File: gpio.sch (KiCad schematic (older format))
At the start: 1 part, among them U1 LFE5U-85F-6BG381C

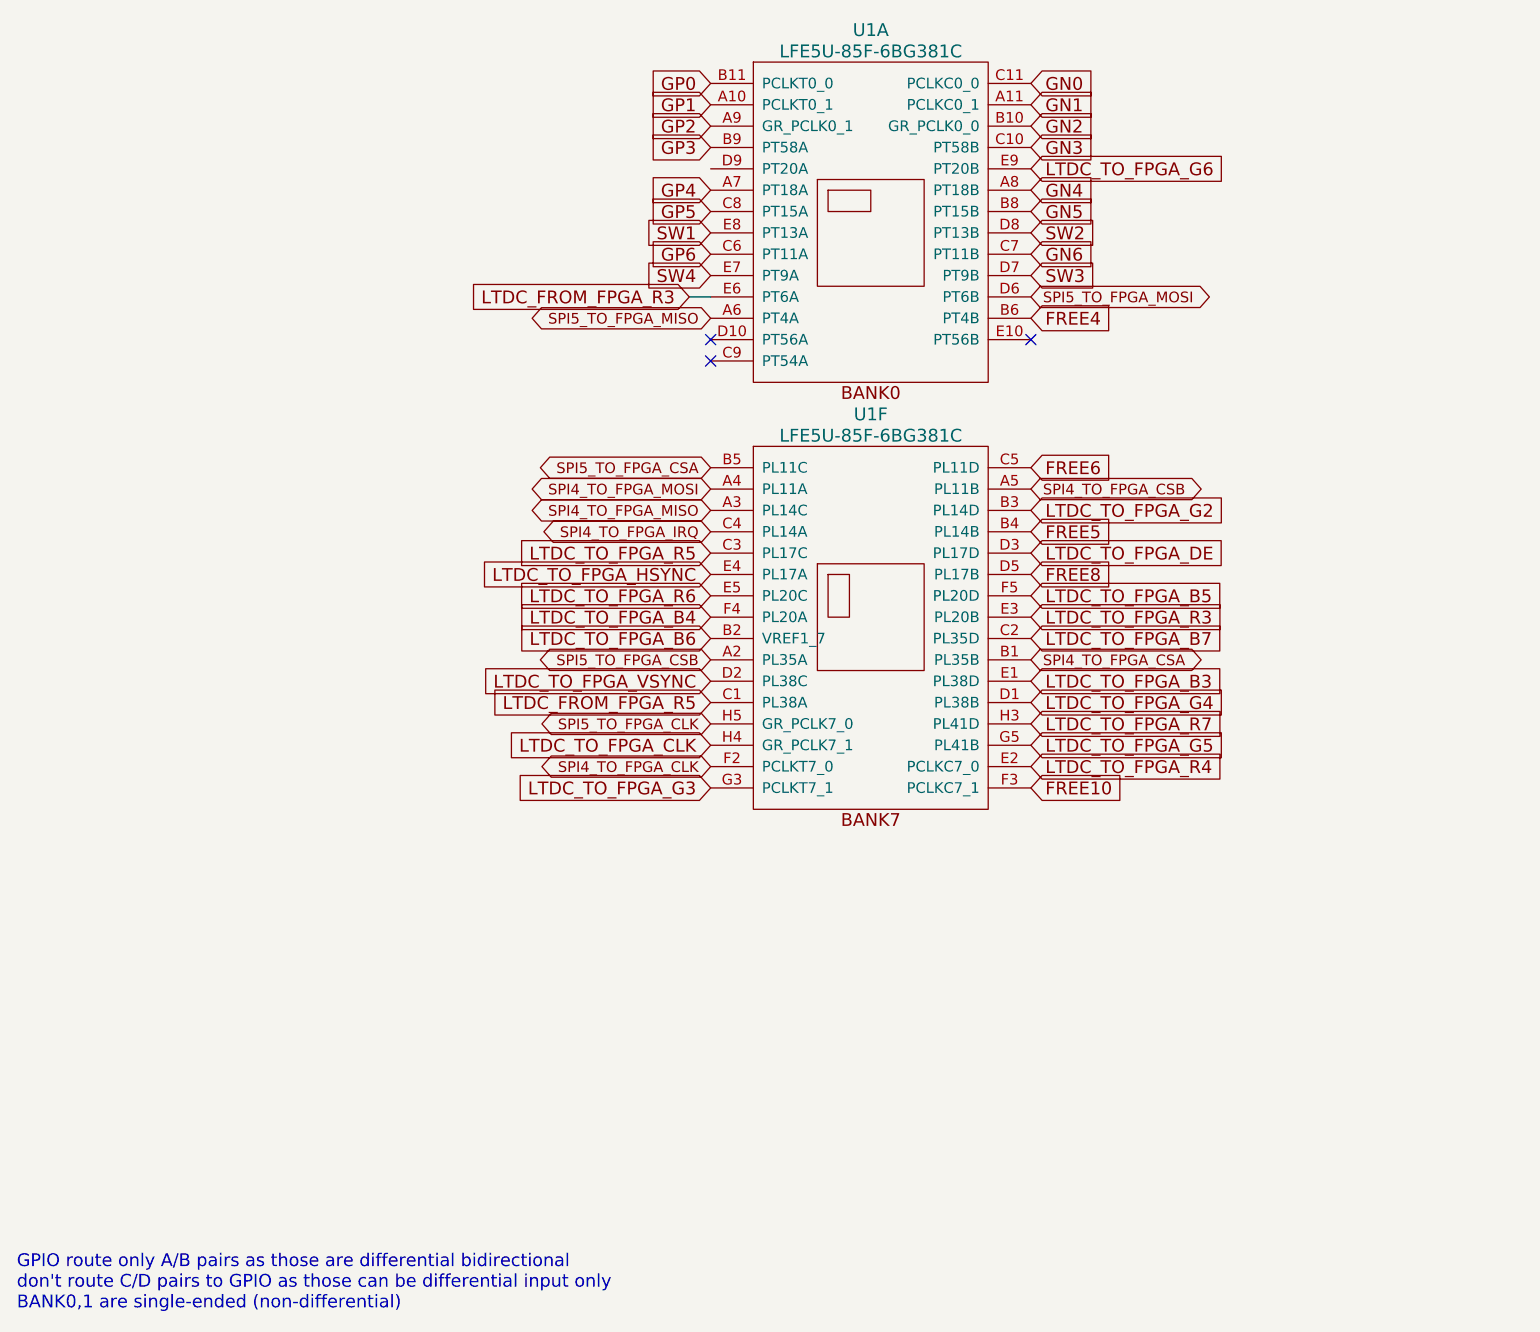
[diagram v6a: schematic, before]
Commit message: Adding SPI from FPGA
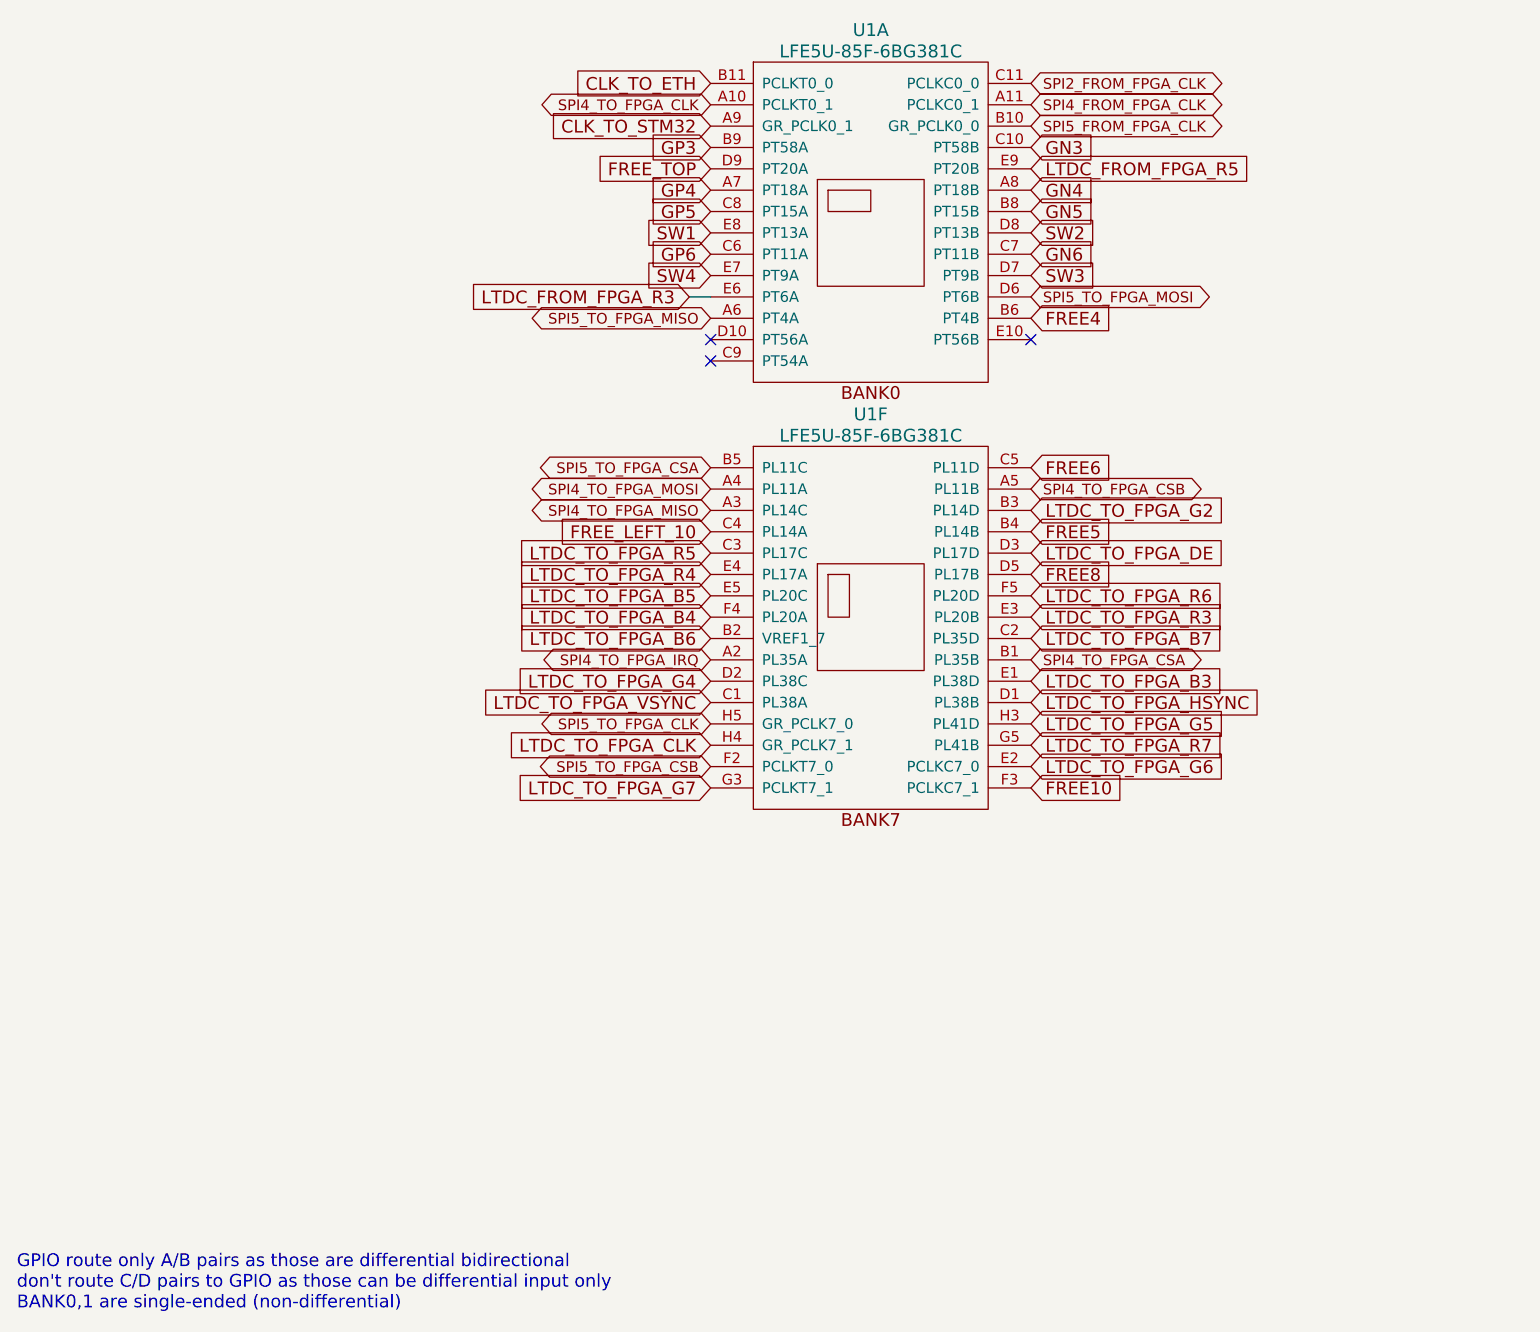
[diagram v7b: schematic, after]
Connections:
- net GP1 is gone; now on net SPI4_TO_FPGA_CLK: U1.A10 (PCLKT0_1)
- net LTDC_FROM_FPGA_R5: now also U1.E9 (PT20B); no longer U1.C1 (PL38A)
- net LTDC_TO_FPGA_B5: now also U1.E5 (PL20C); no longer U1.F5 (PL20D)
- net LTDC_TO_FPGA_G4: now also U1.D2 (PL38C); no longer U1.D1 (PL38B)
- net LTDC_TO_FPGA_G5: now also U1.H3 (PL41D); no longer U1.G5 (PL41B)
- net LTDC_TO_FPGA_G6: now also U1.E2 (PCLKC7_0); no longer U1.E9 (PT20B)
- net LTDC_TO_FPGA_HSYNC: now also U1.D1 (PL38B); no longer U1.E4 (PL17A)
- net LTDC_TO_FPGA_R4: now also U1.E4 (PL17A); no longer U1.E2 (PCLKC7_0)
- net LTDC_TO_FPGA_R6: now also U1.F5 (PL20D); no longer U1.E5 (PL20C)
- net LTDC_TO_FPGA_R7: now also U1.G5 (PL41B); no longer U1.H3 (PL41D)
- net LTDC_TO_FPGA_VSYNC: now also U1.C1 (PL38A); no longer U1.D2 (PL38C)
- net SPI4_TO_FPGA_CLK: no longer U1.F2 (PCLKT7_0)
- net SPI4_TO_FPGA_IRQ: now also U1.A2 (PL35A); no longer U1.C4 (PL14A)
- net SPI5_TO_FPGA_CSB: now also U1.F2 (PCLKT7_0); no longer U1.A2 (PL35A)
- net FREE_TOP: now reaches U1.D9 (PT20A)
- net GN0 renamed SPI2_FROM_FPGA_CLK
- net GN1 renamed SPI4_FROM_FPGA_CLK
- net GN2 renamed SPI5_FROM_FPGA_CLK
- net GP0 renamed CLK_TO_ETH
- net GP2 renamed CLK_TO_STM32
- net LTDC_TO_FPGA_G3 renamed LTDC_TO_FPGA_G7
- new net FREE_LEFT_10: U1.C4 (PL14A)
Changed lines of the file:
@@
 Text GLabel 4200 2600 0    60   Input ~ 0
 GP6
-Text GLabel 5700 1800 2    60   Input ~ 0
-GN0
-Text GLabel 5700 1900 2    60   Input ~ 0
-GN1
-Text GLabel 5700 2000 2    60   Input ~ 0
-GN2
 Text GLabel 5700 2300 2    60   Input ~ 0
 GN4
 Text GLabel 4200 1800 0    60   Input ~ 0
-GP0
-Text GLabel 4200 1900 0    60   Input ~ 0
-GP1
+CLK_TO_ETH
 Text GLabel 4200 2000 0    60   Input ~ 0
-GP2
+CLK_TO_STM32
 Text GLabel 4200 2300 0    60   Input ~ 0
 GP4
@@
 Text GLabel 5700 4300 2    60   Input ~ 0
 LTDC_TO_FPGA_R3
-Text GLabel 5700 5000 2    60   Input ~ 0
+Text GLabel 4200 4100 0    60   Input ~ 0
 LTDC_TO_FPGA_R4
 Text GLabel 4200 4000 0    60   Input ~ 0
 LTDC_TO_FPGA_R5
-Text GLabel 4200 4200 0    60   Input ~ 0
+Text GLabel 5700 4200 2    60   Input ~ 0
 LTDC_TO_FPGA_R6
+Text GLabel 5700 4900 2    60   Input ~ 0
+LTDC_TO_FPGA_R7
+Text GLabel 4200 4600 0    60   Input ~ 0
+LTDC_TO_FPGA_G4
 Text GLabel 5700 4800 2    60   Input ~ 0
-LTDC_TO_FPGA_R7
-Text GLabel 4200 5100 0    60   Input ~ 0
-LTDC_TO_FPGA_G3
-Text GLabel 5700 4700 2    60   Input ~ 0
-LTDC_TO_FPGA_G4
-Text GLabel 5700 4900 2    60   Input ~ 0
 LTDC_TO_FPGA_G5
-Text GLabel 5700 2200 2    60   Input ~ 0
+Text GLabel 5700 5000 2    60   Input ~ 0
 LTDC_TO_FPGA_G6
 Text GLabel 5700 4400 2    60   Input ~ 0
@@
 Text GLabel 4200 4400 0    60   Input ~ 0
 LTDC_TO_FPGA_B6
-Text GLabel 5700 4200 2    60   Input ~ 0
+Text GLabel 4200 4200 0    60   Input ~ 0
 LTDC_TO_FPGA_B5
 Text GLabel 4200 4300 0    60   Input ~ 0
@@
 Text GLabel 5700 4000 2    60   Input ~ 0
 LTDC_TO_FPGA_DE
-Text GLabel 4200 4100 0    60   Input ~ 0
+Text GLabel 5700 4700 2    60   Input ~ 0
 LTDC_TO_FPGA_HSYNC
-Text GLabel 4200 4600 0    60   Input ~ 0
+Text GLabel 4200 4700 0    60   Input ~ 0
 LTDC_TO_FPGA_VSYNC
 Text GLabel 4100 2800 0    60   Input ~ 0
@@
 Wire Wire Line
 	4100 2800 4200 2800
-Text GLabel 4200 4700 0    60   Input ~ 0
+Text GLabel 5700 2200 2    60   Input ~ 0
 LTDC_FROM_FPGA_R5
 Text GLabel 5700 2900 2    60   Input ~ 0
 FREE4
-Text GLabel 5700 3600 2    60   Input ~ 0
-FREE6
-Text GLabel 5700 4100 2    60   Input ~ 0
-FREE8
-Text GLabel 5700 5100 2    60   Input ~ 0
-FREE10
-Text GLabel 4200 5000 0    50   BiDi ~ 0
-SPI4_TO_FPGA_CLK
 Text GLabel 5700 3700 2    50   BiDi ~ 0
 SPI4_TO_FPGA_CSB
@@
 Text GLabel 5700 2800 2    50   BiDi ~ 0
 SPI5_TO_FPGA_MOSI
-Text GLabel 4200 4500 0    50   BiDi ~ 0
+Text GLabel 4200 5000 0    50   BiDi ~ 0
 SPI5_TO_FPGA_CSB
 Text GLabel 5700 4500 2    50   BiDi ~ 0
@@
 Text GLabel 4200 3800 0    50   BiDi ~ 0
 SPI4_TO_FPGA_MISO
-Text GLabel 4200 3900 0    50   BiDi ~ 0
+Text GLabel 4200 4500 0    50   BiDi ~ 0
 SPI4_TO_FPGA_IRQ
+Text GLabel 4200 2200 0    60   Input ~ 0
+FREE_TOP
+Text GLabel 4200 5100 0    60   Input ~ 0
+LTDC_TO_FPGA_G7
+Text GLabel 4200 1900 0    50   BiDi ~ 0
+SPI4_TO_FPGA_CLK
+Text GLabel 4200 3900 0    60   Input ~ 0
+FREE_LEFT_10
+Text GLabel 5700 5100 2    60   Input ~ 0
+FREE10
+Text GLabel 5700 4100 2    60   Input ~ 0
+FREE8
 Text GLabel 5700 3900 2    60   Input ~ 0
 FREE5
+Text GLabel 5700 3600 2    60   Input ~ 0
+FREE6
+Text GLabel 5700 2000 2    50   BiDi ~ 0
+SPI5_FROM_FPGA_CLK
+Text GLabel 5700 1900 2    50   BiDi ~ 0
+SPI4_FROM_FPGA_CLK
+Text GLabel 5700 1800 2    50   BiDi ~ 0
+SPI2_FROM_FPGA_CLK
 $EndSCHEMATC

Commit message: Routing FPGA to LCD
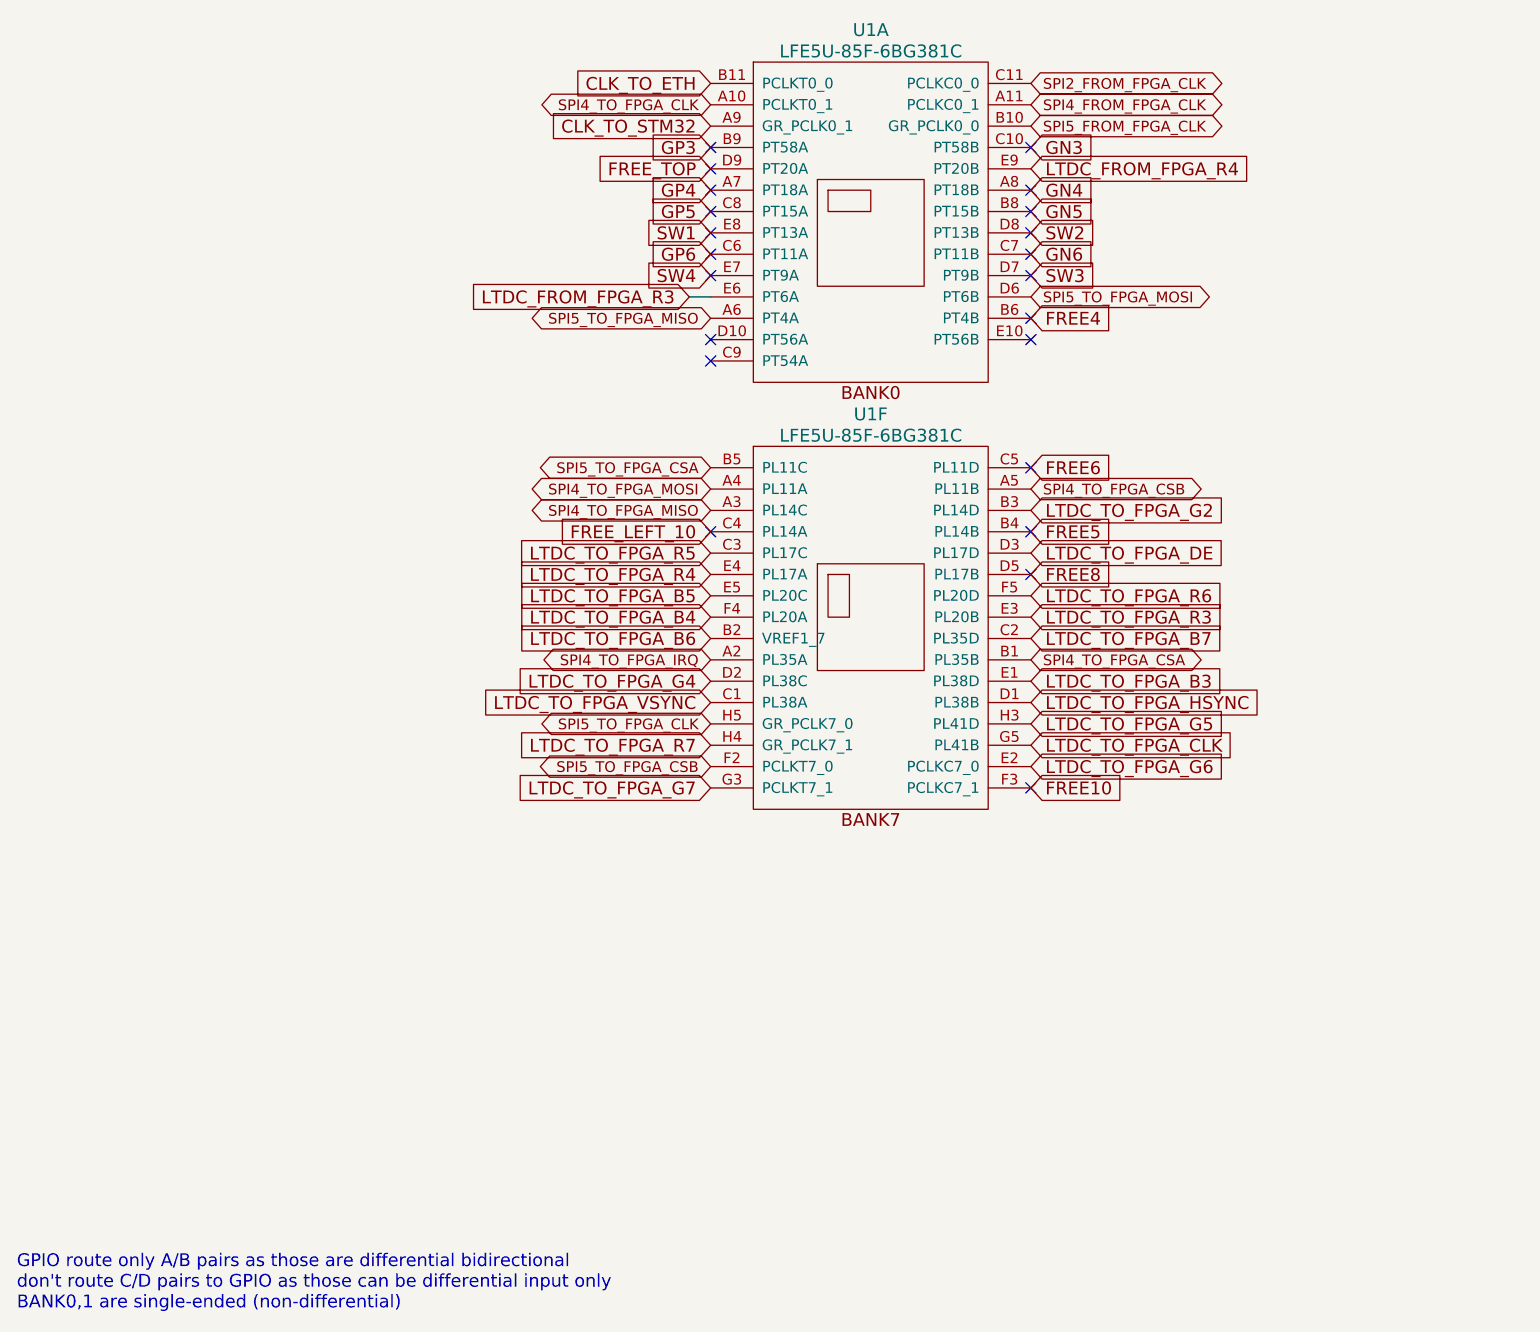
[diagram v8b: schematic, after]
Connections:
- net LTDC_TO_FPGA_CLK: now also U1.G5 (PL41B); no longer U1.H4 (GR_PCLK7_1)
- net LTDC_TO_FPGA_R7: now also U1.H4 (GR_PCLK7_1); no longer U1.G5 (PL41B)
- net LTDC_FROM_FPGA_R5 renamed LTDC_FROM_FPGA_R4
- no-connect marks 3 -> 22
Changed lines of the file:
@@
 Text GLabel 5700 4200 2    60   Input ~ 0
 LTDC_TO_FPGA_R6
-Text GLabel 5700 4900 2    60   Input ~ 0
+Text GLabel 4200 4900 0    60   Input ~ 0
 LTDC_TO_FPGA_R7
 Text GLabel 4200 4600 0    60   Input ~ 0
@@
 Text GLabel 5700 3800 2    60   Input ~ 0
 LTDC_TO_FPGA_G2
-Text GLabel 4200 4900 0    60   Input ~ 0
+Text GLabel 5700 4900 2    60   Input ~ 0
 LTDC_TO_FPGA_CLK
 Text GLabel 5700 4000 2    60   Input ~ 0
@@
 Wire Wire Line
 	4100 2800 4200 2800
-Text GLabel 5700 2200 2    60   Input ~ 0
-LTDC_FROM_FPGA_R5
 Text GLabel 5700 2900 2    60   Input ~ 0
 FREE4
@@
 Text GLabel 5700 1800 2    50   BiDi ~ 0
 SPI2_FROM_FPGA_CLK
+NoConn ~ 4200 2100
+NoConn ~ 4200 2200
+NoConn ~ 4200 2300
+NoConn ~ 4200 2400
+NoConn ~ 4200 2500
+NoConn ~ 4200 2600
+NoConn ~ 4200 2700
+NoConn ~ 5700 2900
+NoConn ~ 5700 2700
+NoConn ~ 5700 2600
+NoConn ~ 5700 2500
+NoConn ~ 5700 2400
+NoConn ~ 5700 2300
+NoConn ~ 5700 2100
+NoConn ~ 4200 3900
+NoConn ~ 5700 5100
+NoConn ~ 5700 4100
+NoConn ~ 5700 3900
+NoConn ~ 5700 3600
+Text GLabel 5700 2200 2    60   Input ~ 0
+LTDC_FROM_FPGA_R4
 $EndSCHEMATC
